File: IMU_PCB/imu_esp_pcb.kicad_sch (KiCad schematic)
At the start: 22 parts, among them J1 Conn_01x02_Pin, J2 Conn_01x05_Pin, U1 MPU-6050, U2 ESP32-C3-WROOM-02, U3 PTS647SM38SMTR2LFS, U4 XC6206P332MR-G, U5 1N5819HW-7-F

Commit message: Updated Schematic
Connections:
- net RXD: now also U2.11 (IO20/RXD); no longer U2.12 (IO21/TXD)
- net TXD: now also U2.12 (IO21/TXD); no longer U2.11 (IO20/RXD)
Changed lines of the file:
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@@
 	(global_label "TXD"
 		(shape input)
-		(at 167.64 41.91 0)
+		(at 167.64 44.45 0)
 		(fields_autoplaced yes)
 		(effects
@@
 		)
 		(property "Intersheetrefs" "${INTERSHEET_REFS}"
-			(at 174.0723 41.91 0)
+			(at 174.0723 44.45 0)
 			(effects
 				(font
@@
 	(global_label "RXD"
 		(shape input)
-		(at 167.64 44.45 0)
+		(at 167.64 41.91 0)
 		(fields_autoplaced yes)
 		(effects
@@
 		)
 		(property "Intersheetrefs" "${INTERSHEET_REFS}"
-			(at 174.3747 44.45 0)
+			(at 174.3747 41.91 0)
 			(effects
 				(font

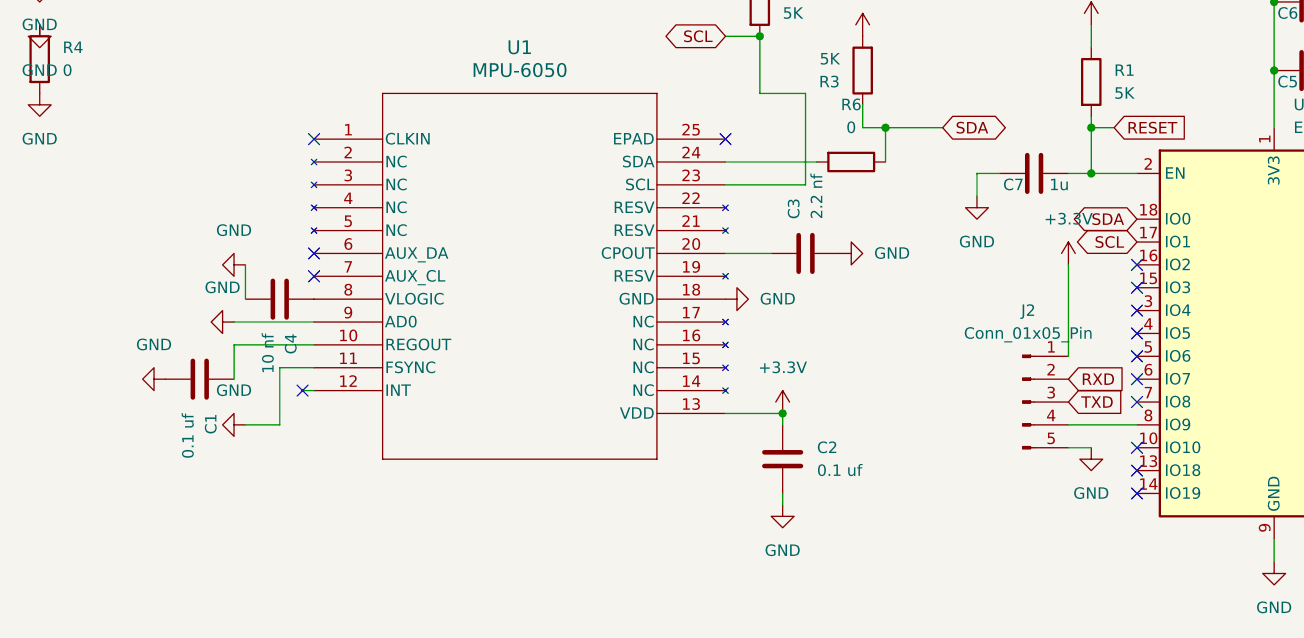
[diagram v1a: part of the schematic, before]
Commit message: Fixing PCB files from root
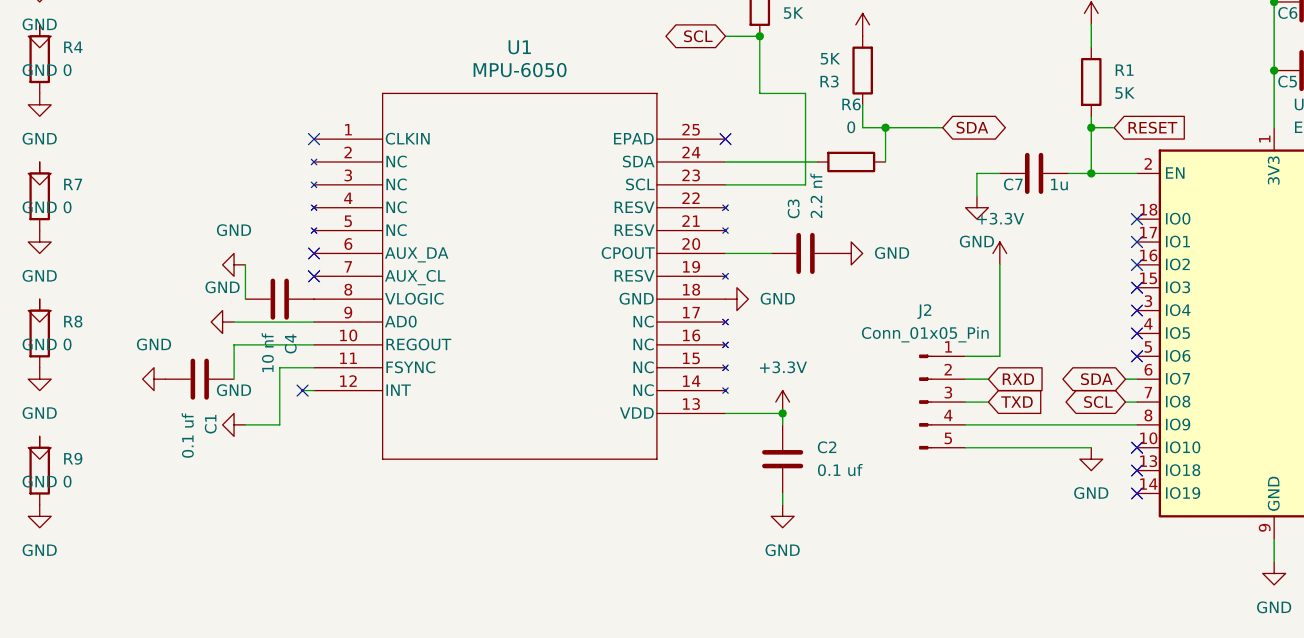
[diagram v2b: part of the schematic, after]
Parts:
- added R7, R8, R9: 0, Resistor_SMD:R_0805_2012Metric_Pad1.20x1.40mm_HandSolder, symbol Device:R
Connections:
- net GND: now also R7.1, R7.2, R8.1, R8.2, R9.1, R9.2
- net SCL: now also U2.7 (IO8); no longer U2.17 (IO1)
- net SDA: now also U2.6 (IO7); no longer U2.18 (IO0)
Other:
- moved on the sheet: J2
